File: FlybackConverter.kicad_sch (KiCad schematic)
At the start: 36 parts, among them J1 USB_C_Receptacle_PowerOnly_6P, T1 Transformer_1P_2S, U1 LNK6428K, U2 TPS25820DSST

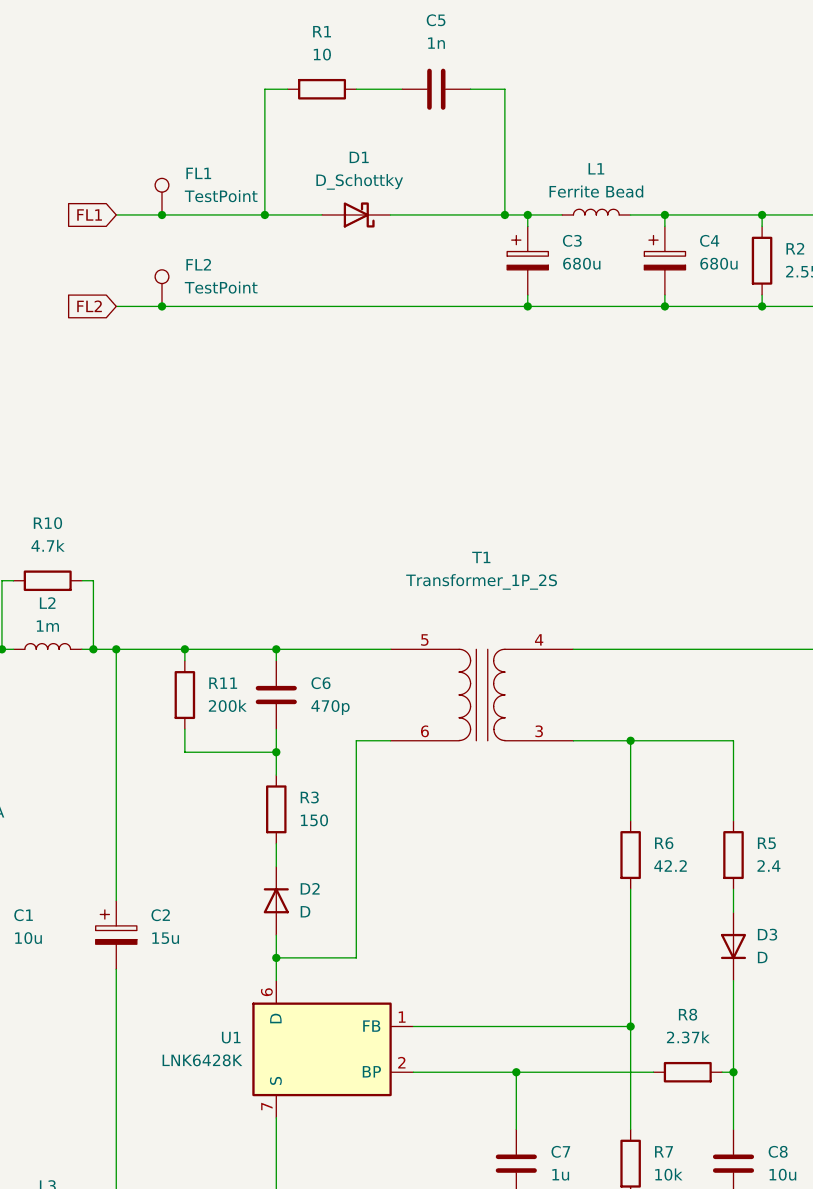
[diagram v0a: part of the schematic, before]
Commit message: 可変抵抗接続用に配線を引き出せる穴を追加 fix #2
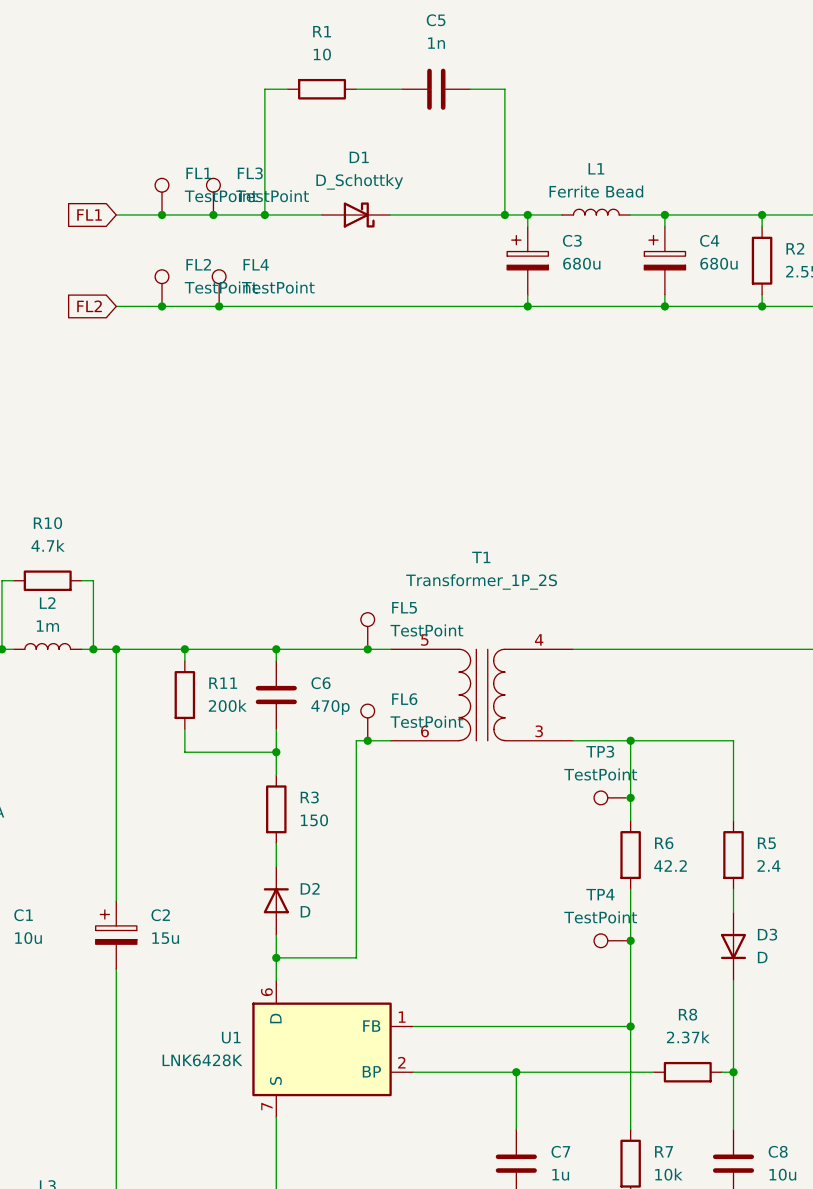
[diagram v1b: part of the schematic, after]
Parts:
- added FL3, FL4, FL5, FL6, TP3, TP4: TestPoint, TestPoint:TestPoint_Loop_D1.80mm_Drill1.0mm_Beaded, symbol Connector:TestPoint
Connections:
- net FL1: now also FL3.1
- net FL2: now also FL4.1
- net at C2.1, C6.1, L2.2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: now also FL5.1
- net at R6.2, R7.1, U1.1 (FB): now also TP4.1
- net at D2.2 (A), T1.6 (AB), U1.6 (D): now also FL6.1
- net at R5.1, R6.1, T1.3 (SA): now also TP3.1
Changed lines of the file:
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@@
 (kicad_sch (version 20230121) (generator eeschema)
   (paper "A4")
+  (junction (at 137.16 113.03) (diameter 0) (color 0 0 0 0)
+  )
   (junction (at 137.16 161.29) (diameter 0) (color 0 0 0 0)
   )
+  (junction (at 137.16 128.905) (diameter 0) (color 0 0 0 0)
+  )
   (junction (at 148.59 161.29) (diameter 0) (color 0 0 0 0)
   )
@@
   (junction (at 67.31 96.52) (diameter 0) (color 0 0 0 0)
   )
+  (junction (at 107.95 106.68) (diameter 0) (color 0 0 0 0)
+  )
   (junction (at 124.46 161.29) (diameter 0) (color 0 0 0 0)
   )
@@
   (junction (at 97.79 107.95) (diameter 0) (color 0 0 0 0)
   )
+  (junction (at 91.44 58.42) (diameter 0) (color 0 0 0 0)
+  )
   (junction (at 77.47 96.52) (diameter 0) (color 0 0 0 0)
   )
@@
   (junction (at 164.465 58.42) (diameter 0) (color 0 0 0 0)
   )
+  (junction (at 90.805 48.26) (diameter 0) (color 0 0 0 0)
+  )
   (junction (at 80.01 161.29) (diameter 0) (color 0 0 0 0)
   )
   (junction (at 96.52 48.26) (diameter 0) (color 0 0 0 0)
   )
+  (junction (at 107.95 96.52) (diameter 0) (color 0 0 0 0)
+  )
   (junction (at 168.91 46.99) (diameter 0) (color 0 0 0 0)
   )
@@
   (junction (at 168.91 44.45) (diameter 0) (color 0 0 0 0)
   )
+  (wire (pts (xy 91.44 58.42) (xy 125.73 58.42))
+    (stroke (width 0) (type default))
+  )
   (wire (pts (xy 220.98 69.85) (xy 228.6 69.85))
     (stroke (width 0) (type default))
@@
     (stroke (width 0) (type default))
   )
+  (wire (pts (xy 90.805 48.26) (xy 85.09 48.26))
+    (stroke (width 0) (type default))
+  )
   (wire (pts (xy 68.58 96.52) (xy 67.31 96.52))
     (stroke (width 0) (type default))
@@
     (stroke (width 0) (type default))
   )
+  (wire (pts (xy 137.16 113.03) (xy 137.16 115.57))
+    (stroke (width 0) (type default))
+  )
   (wire (pts (xy 196.215 53.34) (xy 205.74 53.34))
     (stroke (width 0) (type default))
@@
     (stroke (width 0) (type default))
   )
-  (wire (pts (xy 97.79 96.52) (xy 110.49 96.52))
-    (stroke (width 0) (type default))
-  )
-  (wire (pts (xy 85.09 58.42) (xy 125.73 58.42))
+  (wire (pts (xy 97.79 96.52) (xy 107.95 96.52))
+    (stroke (width 0) (type default))
+  )
+  (wire (pts (xy 85.09 58.42) (xy 91.44 58.42))
     (stroke (width 0) (type default))
   )
@@
     (stroke (width 0) (type default))
   )
-  (wire (pts (xy 106.68 106.68) (xy 110.49 106.68))
+  (wire (pts (xy 137.16 128.905) (xy 137.16 123.19))
+    (stroke (width 0) (type default))
+  )
+  (wire (pts (xy 106.68 106.68) (xy 107.95 106.68))
     (stroke (width 0) (type default))
   )
@@
     (stroke (width 0) (type default))
   )
-  (wire (pts (xy 96.52 48.26) (xy 85.09 48.26))
+  (wire (pts (xy 96.52 48.26) (xy 90.805 48.26))
     (stroke (width 0) (type default))
   )
@@
     (stroke (width 0) (type default))
   )
+  (wire (pts (xy 107.95 106.68) (xy 110.49 106.68))
+    (stroke (width 0) (type default))
+  )
   (wire (pts (xy 34.29 135.89) (xy 34.29 138.43))
     (stroke (width 0) (type default))
@@
     (stroke (width 0) (type default))
   )
-  (wire (pts (xy 137.16 138.43) (xy 137.16 123.19))
+  (wire (pts (xy 137.16 138.43) (xy 137.16 128.905))
     (stroke (width 0) (type default))
   )
@@
     (stroke (width 0) (type default))
   )
-  (wire (pts (xy 137.16 106.68) (xy 137.16 115.57))
+  (wire (pts (xy 137.16 106.68) (xy 137.16 113.03))
     (stroke (width 0) (type default))
   )
@@
   )
   (wire (pts (xy 64.77 96.52) (xy 46.99 96.52))
+    (stroke (width 0) (type default))
+  )
+  (wire (pts (xy 107.95 96.52) (xy 110.49 96.52))
     (stroke (width 0) (type default))
   )
@@
     )
   )
+  (symbol (lib_id "Connector:TestPoint") (at 107.95 106.68 0) (unit 1)
+    (in_bom yes) (on_board yes) (dnp no) (fields_autoplaced)
+    (property "Reference" "FL6" (at 110.49 102.108 0)
+      (effects (font (size 1.27 1.27)) (justify left))
+    )
+    (property "Value" "TestPoint" (at 110.49 104.648 0)
+      (effects (font (size 1.27 1.27)) (justify left))
+    )
+    (property "Footprint" "TestPoint:TestPoint_Loop_D1.80mm_Drill1.0mm_Beaded" (at 113.03 106.68 0)
+      (effects (font (size 1.27 1.27)) hide)
+    )
+    (property "Datasheet" "~" (at 113.03 106.68 0)
+      (effects (font (size 1.27 1.27)) hide)
+    )
+    (pin "1")
+    (instances
+      (project "FlybackConverter"
+        (path "/f7ad8aa8-e3ae-4e7c-846c-9c0c6caa5ffd"
+          (reference "FL6") (unit 1)
+        )
+      )
+    )
+  )
   (symbol (lib_id "Device:R") (at 72.39 88.9 90) (unit 1)
     (in_bom yes) (on_board yes) (dnp no) (fields_autoplaced)
@@
     )
   )
+  (symbol (lib_id "Connector:TestPoint") (at 137.16 128.905 90) (unit 1)
+    (in_bom yes) (on_board yes) (dnp no) (fields_autoplaced)
+    (property "Reference" "TP4" (at 133.858 123.825 90)
+      (effects (font (size 1.27 1.27)))
+    )
+    (property "Value" "TestPoint" (at 133.858 126.365 90)
+      (effects (font (size 1.27 1.27)))
+    )
+    (property "Footprint" "TestPoint:TestPoint_Loop_D1.80mm_Drill1.0mm_Beaded" (at 137.16 123.825 0)
+      (effects (font (size 1.27 1.27)) hide)
+    )
+    (property "Datasheet" "~" (at 137.16 123.825 0)
+      (effects (font (size 1.27 1.27)) hide)
+    )
+    (pin "1")
+    (instances
+      (project "FlybackConverter"
+        (path "/f7ad8aa8-e3ae-4e7c-846c-9c0c6caa5ffd"
+          (reference "TP4") (unit 1)
+        )
+      )
+    )
+  )
   (symbol (lib_id "Device:D") (at 148.59 129.54 90) (unit 1)
     (in_bom yes) (on_board yes) (dnp no) (fields_autoplaced)
@@
         (path "/f7ad8aa8-e3ae-4e7c-846c-9c0c6caa5ffd"
           (reference "D3") (unit 1)
+        )
+      )
+    )
+  )
+  (symbol (lib_id "Connector:TestPoint") (at 90.805 48.26 0) (unit 1)
+    (in_bom yes) (on_board yes) (dnp no) (fields_autoplaced)
+    (property "Reference" "FL3" (at 93.345 43.688 0)
+      (effects (font (size 1.27 1.27)) (justify left))
+    )
+    (property "Value" "TestPoint" (at 93.345 46.228 0)
+      (effects (font (size 1.27 1.27)) (justify left))
+    )
+    (property "Footprint" "TestPoint:TestPoint_Loop_D1.80mm_Drill1.0mm_Beaded" (at 95.885 48.26 0)
+      (effects (font (size 1.27 1.27)) hide)
+    )
+    (property "Datasheet" "~" (at 95.885 48.26 0)
+      (effects (font (size 1.27 1.27)) hide)
+    )
+    (pin "1")
+    (instances
+      (project "FlybackConverter"
+        (path "/f7ad8aa8-e3ae-4e7c-846c-9c0c6caa5ffd"
+          (reference "FL3") (unit 1)
         )
       )
@@
     )
   )
+  (symbol (lib_id "Connector:TestPoint") (at 137.16 113.03 90) (unit 1)
+    (in_bom yes) (on_board yes) (dnp no) (fields_autoplaced)
+    (property "Reference" "TP3" (at 133.858 107.95 90)
+      (effects (font (size 1.27 1.27)))
+    )
+    (property "Value" "TestPoint" (at 133.858 110.49 90)
+      (effects (font (size 1.27 1.27)))
+    )
+    (property "Footprint" "TestPoint:TestPoint_Loop_D1.80mm_Drill1.0mm_Beaded" (at 137.16 107.95 0)
+      (effects (font (size 1.27 1.27)) hide)
+    )
+    (property "Datasheet" "~" (at 137.16 107.95 0)
+      (effects (font (size 1.27 1.27)) hide)
+    )
+    (pin "1")
+    (instances
+      (project "FlybackConverter"
+        (path "/f7ad8aa8-e3ae-4e7c-846c-9c0c6caa5ffd"
+          (reference "TP3") (unit 1)
+        )
+      )
+    )
+  )
   (symbol (lib_id "Device:Thermistor") (at 34.29 130.81 0) (unit 1)
     (in_bom yes) (on_board yes) (dnp no) (fields_autoplaced)
@@
         )
       )
+    )
+  )
+  (symbol (lib_id "Connector:TestPoint") (at 91.44 58.42 0) (unit 1)
+    (in_bom yes) (on_board yes) (dnp no) (fields_autoplaced)
+    (property "Reference" "FL4" (at 93.98 53.848 0)
+      (effects (font (size 1.27 1.27)) (justify left))
+    )
+    (property "Value" "TestPoint" (at 93.98 56.388 0)
+      (effects (font (size 1.27 1.27)) (justify left))
+    )
+    (property "Footprint" "TestPoint:TestPoint_Loop_D1.80mm_Drill1.0mm_Beaded" (at 96.52 58.42 0)
+      (effects (font (size 1.27 1.27)) hide)
+    )
+    (property "Datasheet" "~" (at 96.52 58.42 0)
+      (effects (font (size 1.27 1.27)) hide)
+    )
+    (pin "1")
+    (instances
+      (project "FlybackConverter"
+        (path "/f7ad8aa8-e3ae-4e7c-846c-9c0c6caa5ffd"
+          (reference "FL4") (unit 1)
+        )
+      )
+    )
+  )
+  (symbol (lib_id "Connector:TestPoint") (at 107.95 96.52 0) (unit 1)
+    (in_bom yes) (on_board yes) (dnp no) (fields_autoplaced)
+    (property "Reference" "FL5" (at 110.49 91.948 0)
+      (effects (font (size 1.27 1.27)) (justify left))
+    )
+    (property "Value" "TestPoint" (at 110.49 94.488 0)
+      (effects (font (size 1.27 1.27)) (justify left))
+    )
+    (property "Footprint" "TestPoint:TestPoint_Loop_D1.80mm_Drill1.0mm_Beaded" (at 113.03 96.52 0)
+      (effects (font (size 1.27 1.27)) hide)
+    )
+    (property "Datasheet" "~" (at 113.03 96.52 0)
+      (effects (font (size 1.27 1.27)) hide)
+    )
+    (pin "1")
+    (instances
+      (project "FlybackConverter"
+        (path "/f7ad8aa8-e3ae-4e7c-846c-9c0c6caa5ffd"
+          (reference "FL5") (unit 1)
+        )
+      )
